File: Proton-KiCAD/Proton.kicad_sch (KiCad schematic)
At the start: 62 parts, among them J1 USB_C_Receptacle_USB2.0_14P, J2 Conn_01x28_Pin, J4 Conn_01x28_Pin, J6 Conn_02x03_Top_Bottom, SW1 BOOTSEL, SW2 RESET, SW3 LEFT, SW4 RIGHT, U1 W25Q128JVS, U2 NCP1117-3.3_SOT223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

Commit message: Added Buttons and IMU
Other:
- added sheet Peripherals (Peripherals.kicad_sch)

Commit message: Fixed to higherarchical labels
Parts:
- removed R10, R9: 27, Resistor_SMD:R_0402_1005Metric, symbol Device:R
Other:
- note added: "Peripherals (Link)"
- note removed: "Make sure R7 and R8 are close to RP2350"

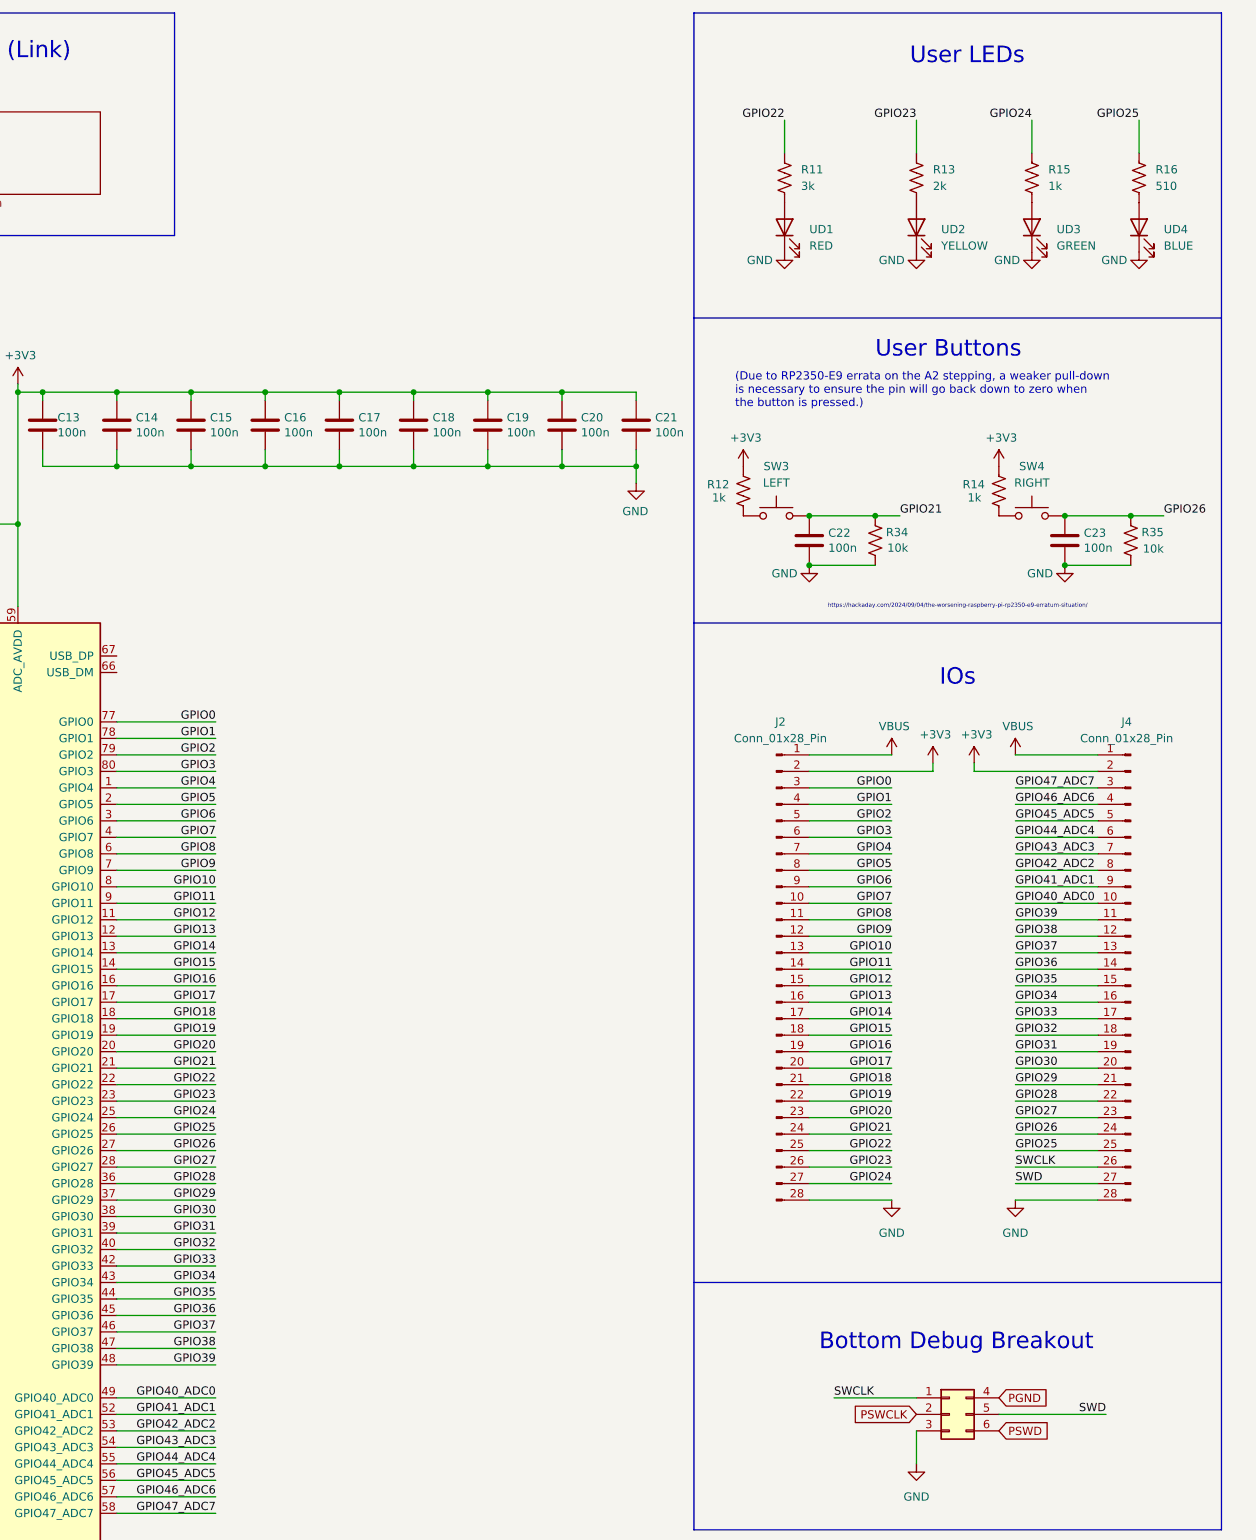
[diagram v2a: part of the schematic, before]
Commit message: Added Pinouts
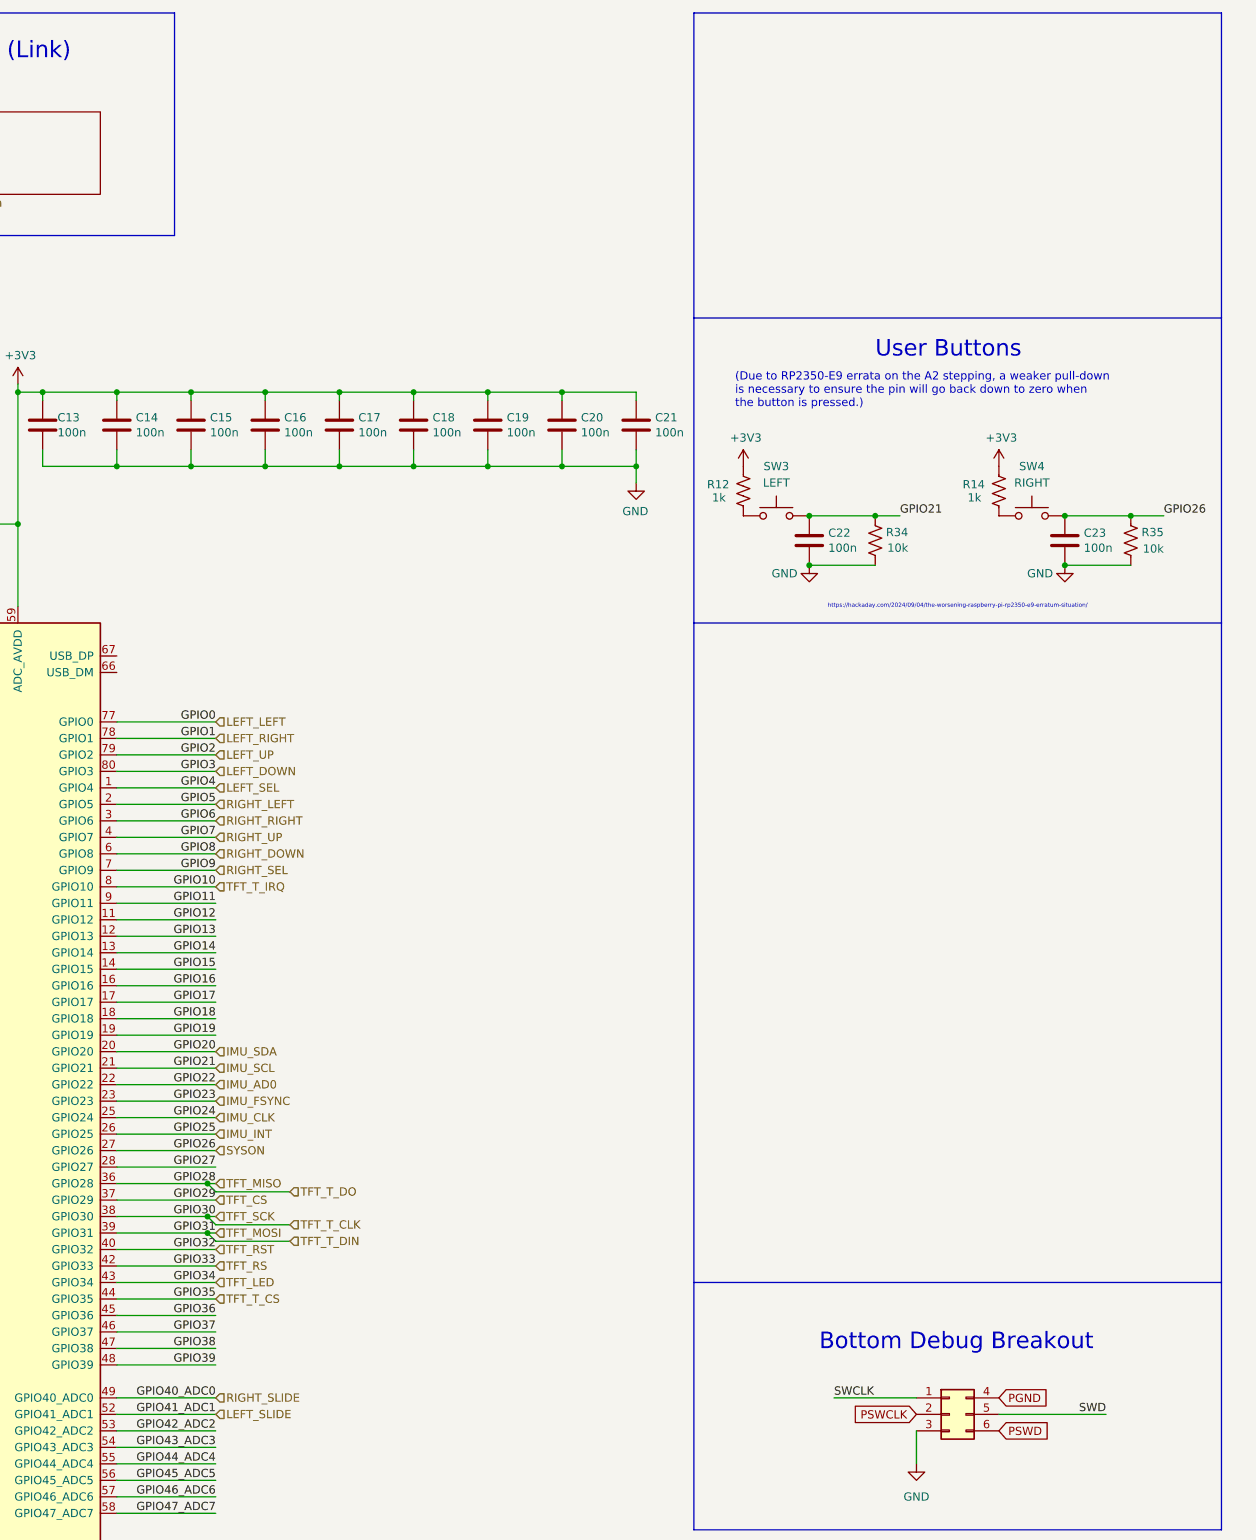
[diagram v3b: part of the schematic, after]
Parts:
- removed J2, J4: Conn_01x28_Pin, Connector_PinHeader_2.54mm:PinHeader_1x28_P2.54mm_Vertical, symbol Connector:Conn_01x28_Pin
- removed R11: 3k, Resistor_SMD:R_0402_1005Metric, symbol Device:R_US
- removed R13: 2k, Resistor_SMD:R_0402_1005Metric, symbol Device:R_US
- removed R15: 1k, Resistor_SMD:R_0402_1005Metric, symbol Device:R_US
- removed R16: 510, Resistor_SMD:R_0402_1005Metric, symbol Device:R_US
- removed UD1: RED, LED_SMD:LED_0805_2012Metric, symbol Device:LED
- removed UD2: YELLOW, LED_SMD:LED_0805_2012Metric, symbol Device:LED
- removed UD3: GREEN, LED_SMD:LED_0805_2012Metric, symbol Device:LED
- removed UD4: BLUE, LED_SMD:LED_0805_2012Metric, symbol Device:LED
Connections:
- net GPIO0 renamed LEFT_LEFT
- net GPIO1 renamed LEFT_RIGHT
- net GPIO10 renamed TFT_T_IRQ
- net GPIO2 renamed LEFT_UP
- net GPIO20 renamed IMU_SDA
- net GPIO21 renamed IMU_SCL
- net GPIO22 renamed IMU_AD0
- net GPIO23 renamed IMU_FSYNC
- net GPIO24 renamed IMU_CLK
- net GPIO25 renamed IMU_INT
- net GPIO26 renamed SYSON
- net GPIO28 renamed TFT_MISO
- net GPIO29 renamed TFT_CS
- net GPIO3 renamed LEFT_DOWN
- net GPIO30 renamed TFT_SCK
- net GPIO31 renamed TFT_MOSI
- net GPIO32 renamed TFT_RST
- net GPIO33 renamed TFT_RS
- net GPIO34 renamed TFT_LED
- net GPIO35 renamed TFT_T_CS
- net GPIO4 renamed LEFT_SEL
- net GPIO40_ADC0 renamed RIGHT_SLIDE
- net GPIO41_ADC1 renamed LEFT_SLIDE
- net GPIO5 renamed RIGHT_LEFT
- net GPIO6 renamed RIGHT_RIGHT
- net GPIO7 renamed RIGHT_UP
- net GPIO8 renamed RIGHT_DOWN
- net GPIO9 renamed RIGHT_SEL
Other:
- note removed: "IOs"
- note removed: "User LEDs"
